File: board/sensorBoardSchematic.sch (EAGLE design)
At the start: 22 parts, among them X1 R141426

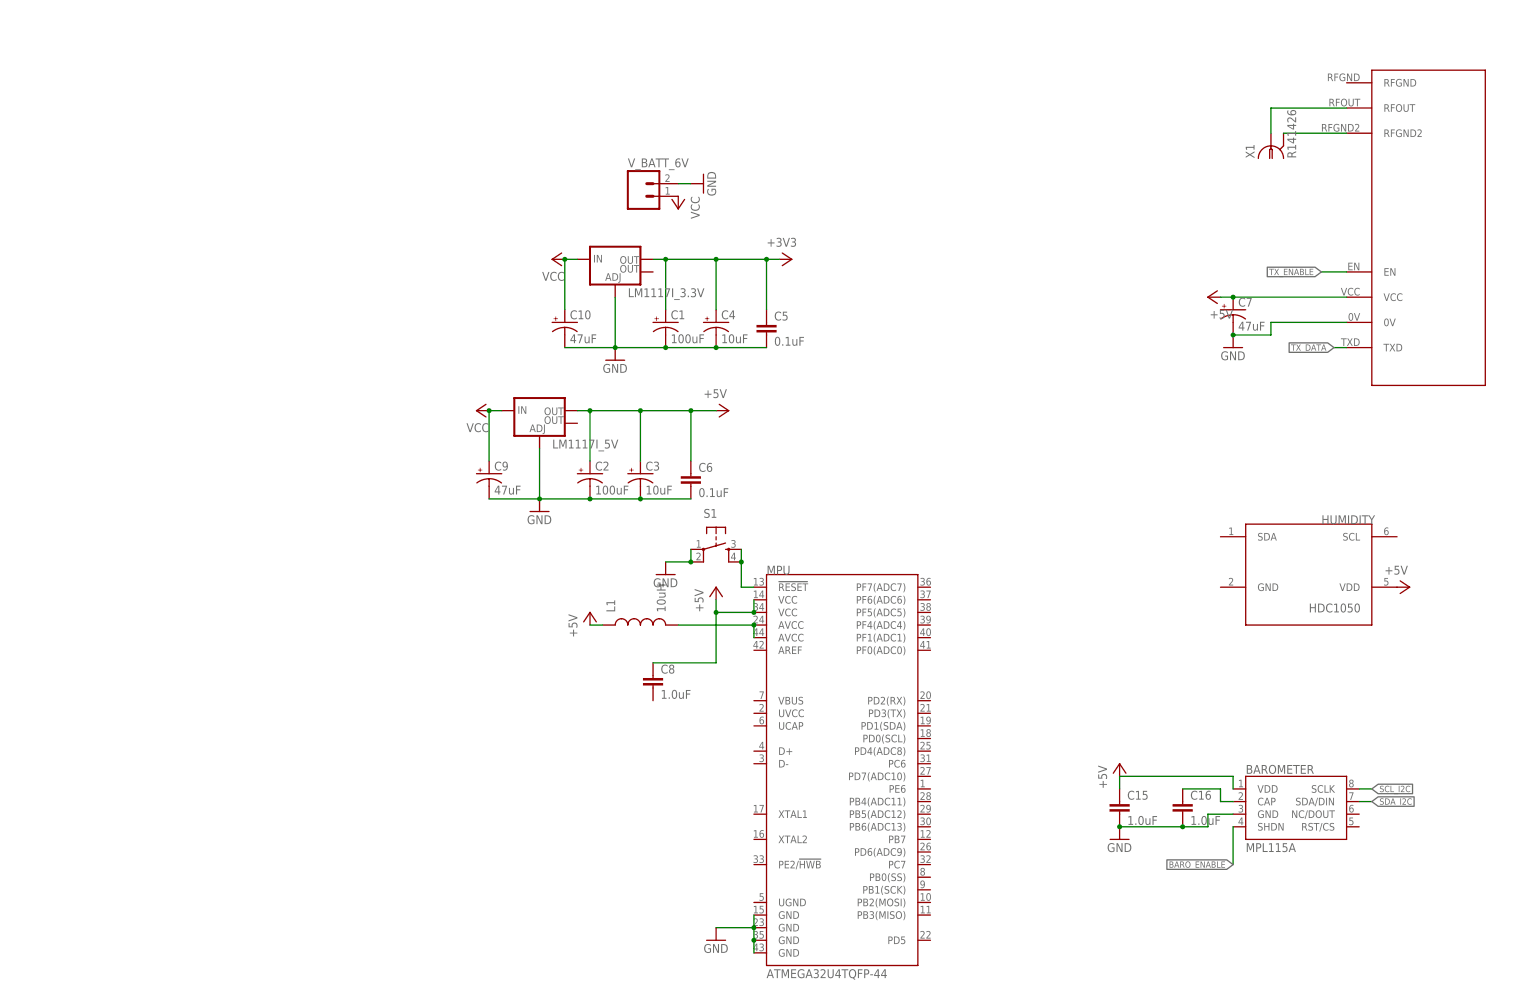
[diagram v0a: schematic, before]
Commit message: huge progress on sensor board schematic; configured USB, ESD isolation for USB, radio (note: need to figure out specs for digital packets from MPU), sensor IC's; analogue sensors and gas sensors need to be configured still
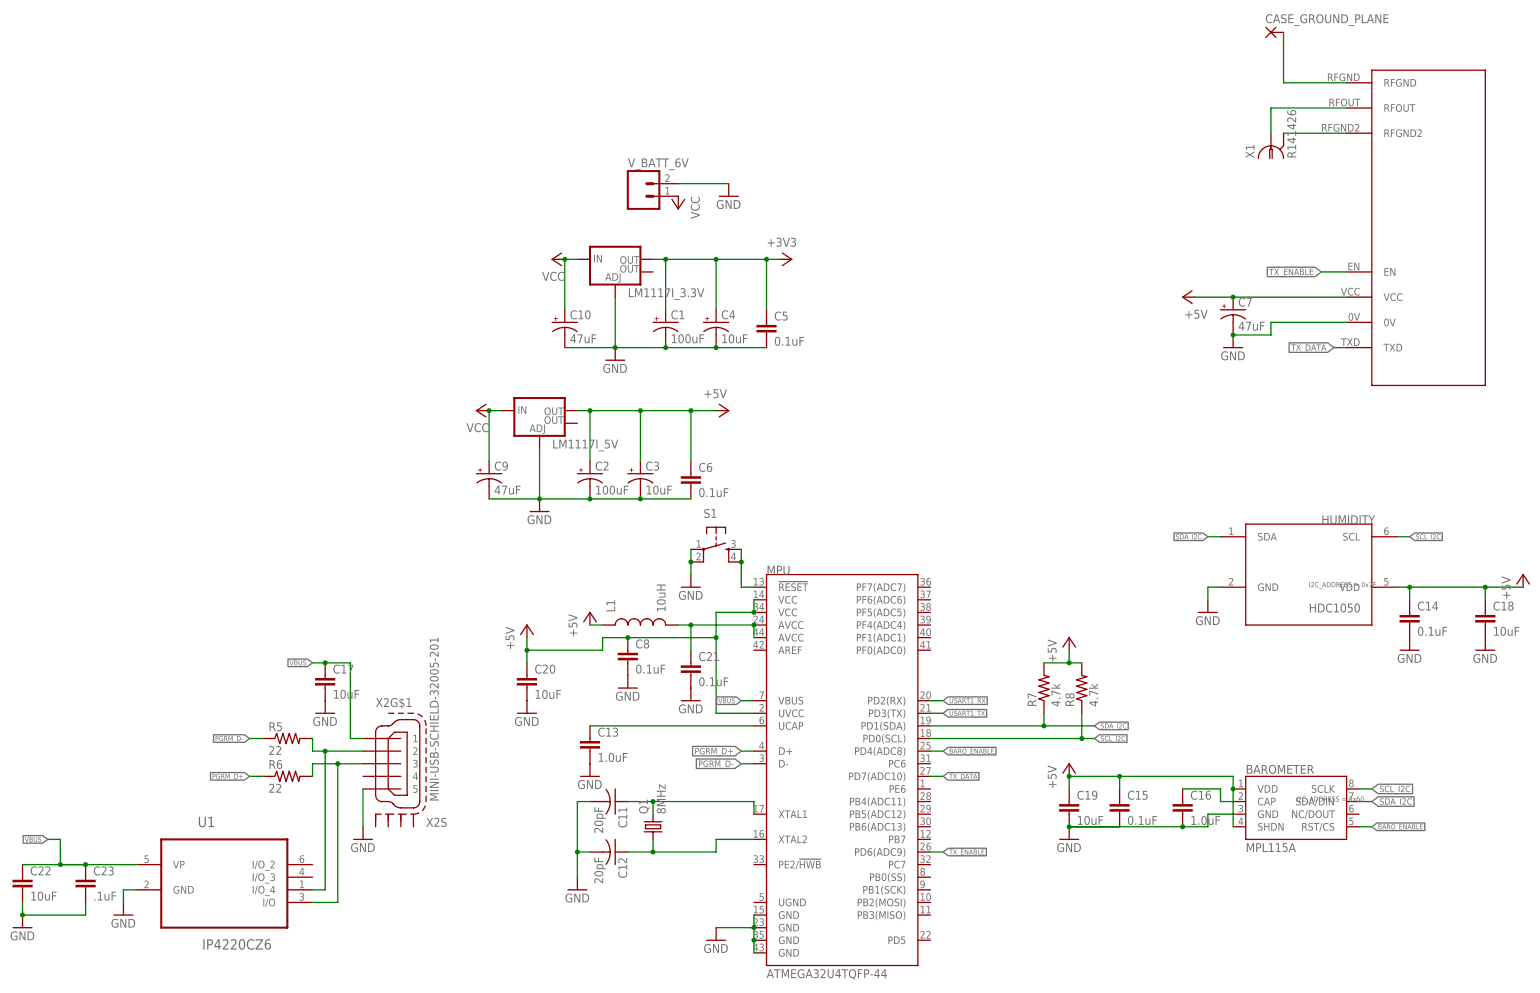
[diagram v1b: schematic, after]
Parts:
- added C11, C12: 20pF, resistor:C-USC0402
- added C13: 1.0uF, SparkFun-Capacitors:1.0UF-16V-10%(0603)
- added C14, C21: 0.1uF, SparkFun-Capacitors:1.0UF-16V-10%(0603)
- added C17, C18, C19, C20, C22: 10uF, SparkFun-Capacitors:1.0UF-16V-10%(0603)
- added C23: .1uF, SparkFun-Capacitors:1.0UF-16V-10%(0603)
- added CASE_GROUND_PLANE: (no value), wirepad:3,81/1,4
- added Q1: 8MHz, crystal:CRYSTALHC49U70
- added R5, R6: 22, SparkFun-Passives:RESISTOR0402-RES
- added R7, R8: 4.7k, SparkFun-Passives:RESISTOR0402-RES
- added U1: IP4220CZ6, NXP_By_element14_Batch_1:IP4220CZ6
- added X2: MINI-USB-SCHIELD-32005-201, con-cypressindustries:MINI-USB-SCHIELD-32005-201
- BAROMETER: I2C_ADDRESS (none) -> 0x60
- C15, C8: value 1.0uF -> 0.1uF
- HUMIDITY: I2C_ADDRESS (none) -> 0x7F
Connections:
- removed net N$5: BAROMETER.VDD
- new net N$10: R5.2, U1.I/O_4, X2G$1.2
- new net N$11: R6.2, U1.I/O, X2G$1.3
- new net N$12: C13.1, MPU.UCAP
- new net N$13: X2G$1.1
- new net N$6: C11.1, MPU.XTAL1, Q1.2
- new net N$8: C12.1, MPU.XTAL2, Q1.1
- new net N$9: CASE_GROUND_PLANE.P, U$1.RFGND
- new net PGRM_D+: MPU.D+, R6.1
- new net PGRM_D-: MPU.D-, R5.1
- new net USART1_RX: MPU.PD2(RX)
- new net USART1_TX: MPU.PD3(TX)
- new net VBUS: C17.1, C22.1, C23.1, MPU.VBUS, U1.VP
- net +5V: now also BAROMETER.SHDN, BAROMETER.VDD, C14.1, C18.1, C19.1, C20.1, MPU.UVCC, R7.2, R8.2
- net BARO_ENABLE: now also BAROMETER.RST/CS, MPU.PD4(ADC8); no longer BAROMETER.SHDN
- net GND: now also C11.2, C12.2, C13.2, C14.2, C17.2, C18.2, C19.2, C20.2, C21.2, C22.2, C23.2, C8.2, HUMIDITY.GND, U1.GND, X2G$1.5
- net N$4: now also C21.1
- net SCL_I2C: now also HUMIDITY.SCL, MPU.PD0(SCL), R8.1
- net SDA_I2C: now also HUMIDITY.SDA, MPU.PD1(SDA), R7.1
- net TX_DATA: now also MPU.PD7(ADC10)
- net TX_ENABLE: now also MPU.PD6(ADC9)
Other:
- moved on the sheet: C8
